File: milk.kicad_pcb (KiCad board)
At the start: 2 copper layers, 20 x 38 mm, 6 parts, among them J1 RGB, J4 RST, K1 KEYSW, K2 KEYSW, U1 ProMicro

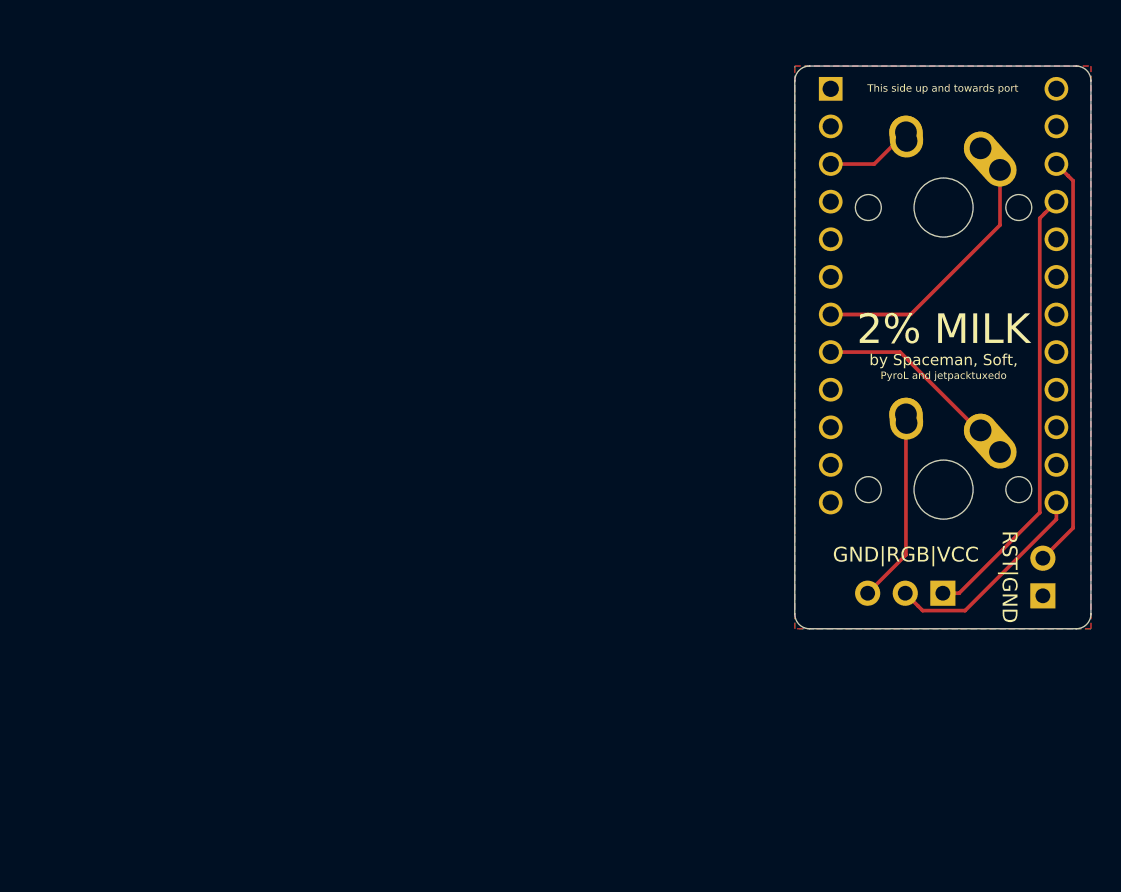
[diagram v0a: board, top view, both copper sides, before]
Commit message: initial schematic and layout (fails drc)
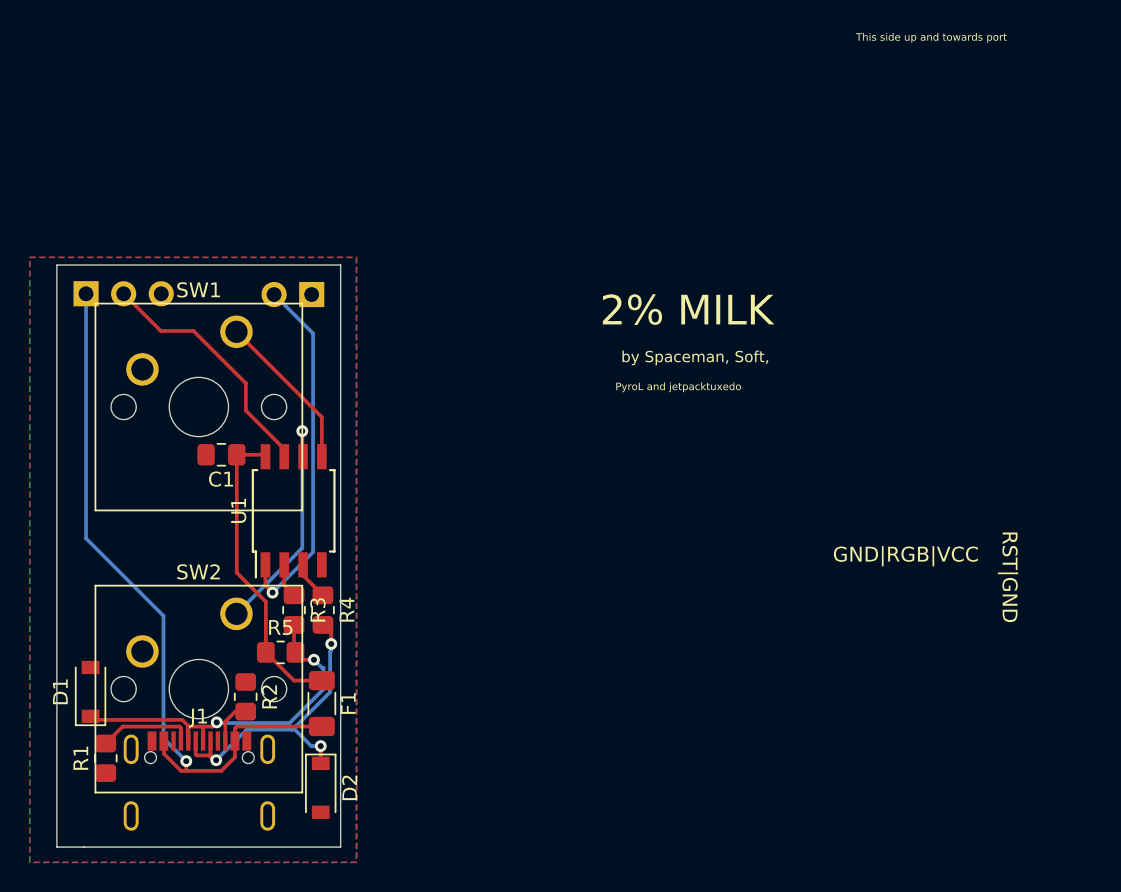
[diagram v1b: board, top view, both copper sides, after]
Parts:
- removed K1, K2: KEYSW, MX_Alps_Hybrid:MX-1U-NoLED
- added C1: 0.1uf, Capacitor_SMD:C_0805_2012Metric_Pad1.18x1.45mm_HandSolder, F.Cu at (181.3, 76.3)
- added D1: 3.6V, Diode_SMD:D_SOD-123, F.Cu at (172.4, 92.3)
- added D2: 3.6V, Diode_SMD:D_SOD-123, F.Cu at (188.0, 98.7)
- added F1: Polyfuse, Resistor_SMD:R_1206_3216Metric_Pad1.30x1.75mm_HandSolder, F.Cu at (188.1, 93.1)
- added J1: USB_C_Receptacle_USB2.0, footprints:Molex_2171800001, F.Cu at (179.8, 103.5)
- added R1: 5.1K, Resistor_SMD:R_0805_2012Metric_Pad1.20x1.40mm_HandSolder, F.Cu at (173.5, 96.7)
- added R2: 5.1K, Resistor_SMD:R_0805_2012Metric_Pad1.20x1.40mm_HandSolder, F.Cu at (182.9, 92.6)
- added R3: 68, Resistor_SMD:R_0805_2012Metric_Pad1.20x1.40mm_HandSolder, F.Cu at (186.2, 86.7)
- added R4: 68, Resistor_SMD:R_0805_2012Metric_Pad1.20x1.40mm_HandSolder, F.Cu at (188.1, 86.7)
- added R5: 1.5K, Resistor_SMD:R_0805_2012Metric_Pad1.20x1.40mm_HandSolder, F.Cu at (185.3, 89.6)
- added SW1: SW_Push, Button_Switch_Keyboard:SW_Cherry_MX_1.00u_PCB, F.Cu at (182.3, 67.9)
- added SW2: SW_Push, Button_Switch_Keyboard:SW_Cherry_MX_1.00u_PCB, F.Cu at (182.3, 87.0)
- U1: value ProMicro -> ATtiny85-20SU; footprint keyboard_parts:ProMicro_NoSilk -> Package_SO:SOIJ-8_5.3x5.3mm_P1.27mm
- moved J3 61.3 mm to (172.1, 65.4), turned to 90 degrees
- moved J2 53.4 mm to (187.4, 65.4), turned to 270 degrees
- moved U1 46.2 mm to (186.2, 80.0), turned to 90 degrees
- moved G*** 17.1 mm to (215.2, 60.5)
- renumbered J4 to J2, J1 to J3
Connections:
- J2 pad 2: /RST -> RST
- J3 pad 2: /RGB -> RGB
- U1 pad 1: Net-(U1-Pad1) -> RST
- U1 pad 2: Net-(U1-Pad2) -> PB3
- U1 pad 3: GND -> PB4
- U1 pad 7: /k1 -> RGB
- U1 pad 8: /k2 -> +5V
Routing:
- net /RST: track 27.9 -> 0.00 mm
- net D-: track 0.00 -> 25.9 mm, vias 0 -> 2
- net RST: track 0.00 -> 24.4 mm, vias 0 -> 1
- net D+: track 0.00 -> 22.0 mm, vias 0 -> 3
- net +5V: track 0.00 -> 20.7 mm
- net GND: track 19.5 -> 0.00 mm
- net VCC: track 30.3 -> 49.4 mm, vias 0 -> 1
- net /k1: track 17.7 -> 0.00 mm
- net RGB: track 0.00 -> 17.3 mm
- net Net-(SW2-Pad1): track 0.00 -> 15.9 mm, vias 0 -> 1
- net /RGB: track 14.4 -> 0.00 mm
- net /k2: track 14.2 -> 0.00 mm
- net Net-(SW1-Pad1): track 0.00 -> 10.8 mm
- net Net-(J1-PadA5): track 0.00 -> 6.47 mm
- net Net-(J1-PadB5): track 0.00 -> 2.97 mm
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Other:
- board size 20 x 38 mm -> 19.2 x 39.3 mm

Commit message: DRC ok
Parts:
- removed G***: LOGO, silks:40logo
- added ?: LOGO, silks:40logo, B.Cu at (181.1, 78.6)
- moved R2 7.81 mm to (180.7, 85.1)
- moved D1 2.84 mm to (173.7, 89.7)
- moved D2 2.84 mm to (189.3, 96.2)
- moved F1 2.84 mm to (189.3, 90.5)
- moved J2 2.84 mm to (188.6, 62.9)
- moved R3 2.84 mm to (187.5, 84.2)
- moved R4 2.84 mm to (189.4, 84.2)
- moved J3 2.84 mm to (173.4, 62.8)
- moved R5 2.84 mm to (186.6, 87.1)
- moved SW2 2.84 mm to (183.6, 84.5)
- moved C1 2.84 mm to (182.5, 73.7)
- moved U1 2.84 mm to (187.4, 77.5)
- moved J1 2.84 mm to (181.1, 101.0)
- moved R1 2.84 mm to (174.7, 94.2)
- moved SW1 2.84 mm to (183.6, 65.4)
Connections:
- J1 pad : (no net) -> GND
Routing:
- net Net-(J1-PadB5): track 2.97 -> 10.8 mm
- net GND: track 0.00 -> 3.28 mm, vias 0 -> 4
- net D-: track 25.9 -> 28.4 mm
- net RST: track 24.4 -> 25.5 mm
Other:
- board text added: "VCC|RGB|GND"
- board text removed: "GND|RGB|VCC"

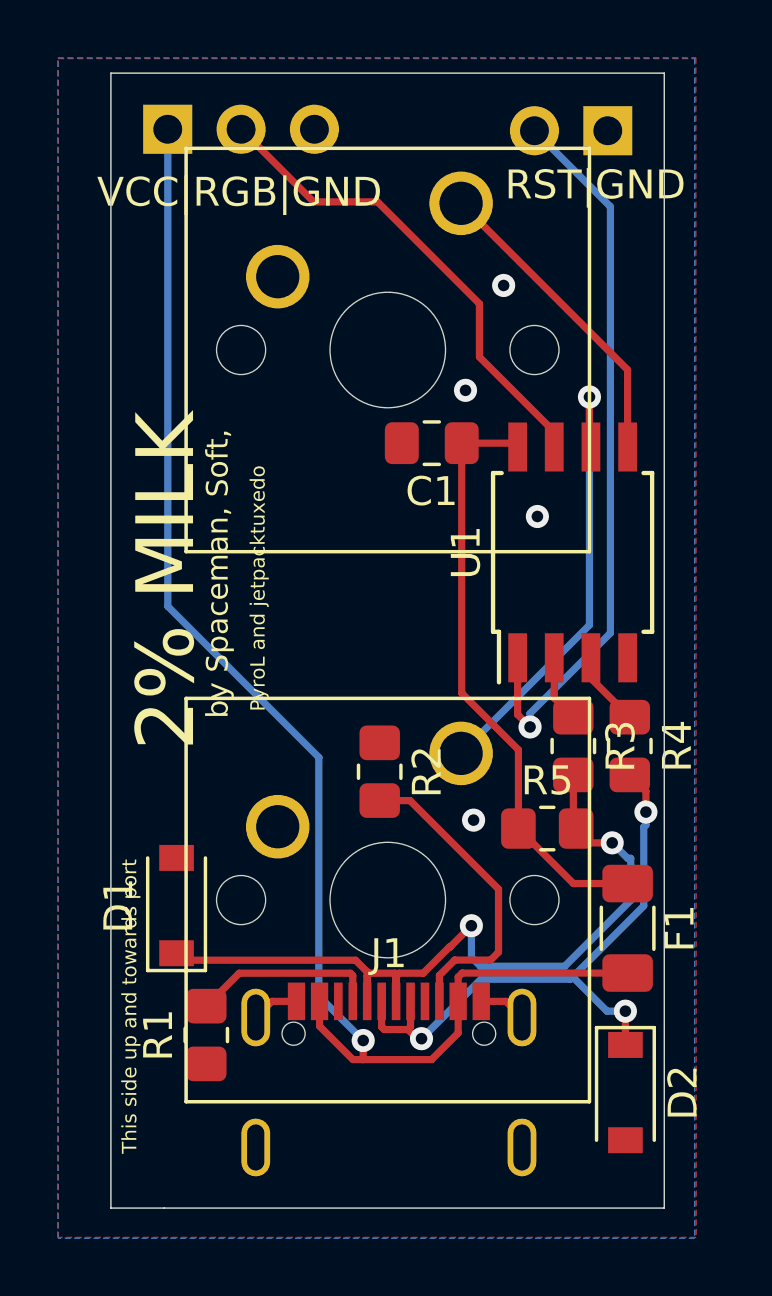
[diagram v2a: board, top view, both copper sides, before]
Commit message: Add programming headers (all over the place... yes)
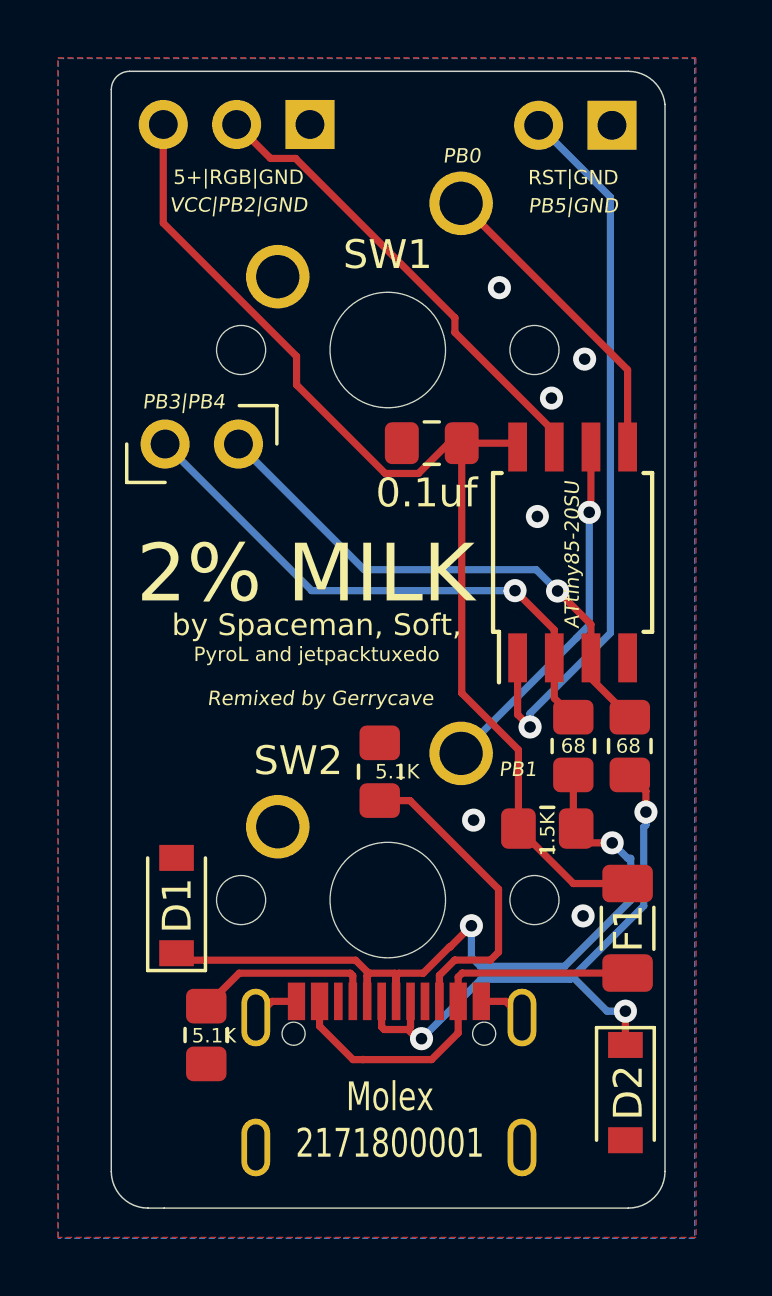
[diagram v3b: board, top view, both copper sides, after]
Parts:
- added J4: PB3|PB4, Connector_PinHeader_2.54mm:PinHeader_1x02_P2.54mm_Vertical, F.Cu at (173.3, 73.7)
- moved J3 4.93 mm to (178.3, 62.7), turned to 270 degrees
- moved J2 0.24 mm to (188.8, 62.7)
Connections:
- J3 pad 1: VCC -> GND
- J3 pad 3: GND -> +5V
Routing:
- net VCC: track 49.4 -> 14.4 mm, vias 1 -> 0
- net +5V: track 20.7 -> 39.2 mm
- net PB3: track 2.33 -> 19.4 mm, vias 0 -> 1
- net PB4: track 2.61 -> 18.6 mm, vias 0 -> 1
- net Net-(SW2-Pad1): track 15.9 -> 13.2 mm
- net RGB: track 17.3 -> 16.8 mm
- net GND: vias 4 -> 6
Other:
- board size 19.2 x 39.3 mm -> 19.2 x 39.4 mm
- rule pad_to_mask_clearance: 0.051 -> 0
- board text added: "0.1uf"
- board text added: "1.5K"
- board text added: "5+|RGB|GND"
- board text added: "5.1K"
- board text added: "68"
- board text added: "ATtiny85-20SU"
- board text added: "Molex 2171800001"
- board text added: "PB0"
- board text added: "PB1"
- board text added: "PB3|PB4"
- board text added: "PB5|GND"
- board text added: "Remixed by Gerrycave"
- board text added: "VCC|PB2|GND"
- board text removed: "This side up and towards port"
- board text removed: "VCC|RGB|GND"

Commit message: Final gerber, rendered images
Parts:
- added .: TestPoint_THTPad_D1.5mm_Drill0.7mm, TestPoint:TestPoint_THTPad_D1.5mm_Drill0.7mm, F.Cu at (180.3, 63.5)
- added .: TestPoint_THTPad_D1.5mm_Drill0.7mm, TestPoint:TestPoint_THTPad_D1.5mm_Drill0.7mm, F.Cu at (177.8, 73.7)
- moved J2 1.15 mm to (188.0, 63.5)
- moved J3 0.98 mm to (177.8, 63.5)
- moved J4 0.60 mm to (172.7, 73.7)
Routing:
- net Net-(SW2-Pad1): track 13.2 -> 26.4 mm
- net Net-(SW1-Pad1): track 10.8 -> 14.8 mm
- net PB4: track 18.6 -> 20.5 mm
- net RGB: track 16.8 -> 18.1 mm
- net PB3: track 19.4 -> 20.6 mm
- net GND: vias 6 -> 9
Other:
- board text added: "PB3|PB4|PB1"
- board text removed: "PB1"
- board text removed: "PB3|PB4"

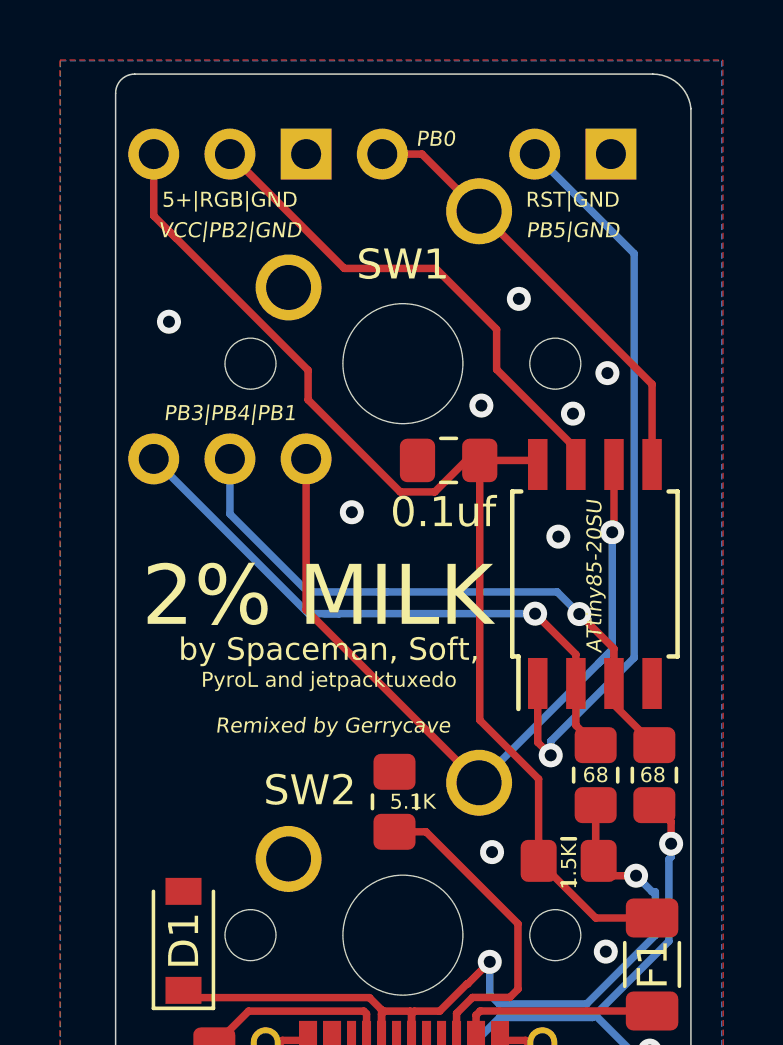
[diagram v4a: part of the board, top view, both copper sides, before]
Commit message: Fix pogo pin tht holes
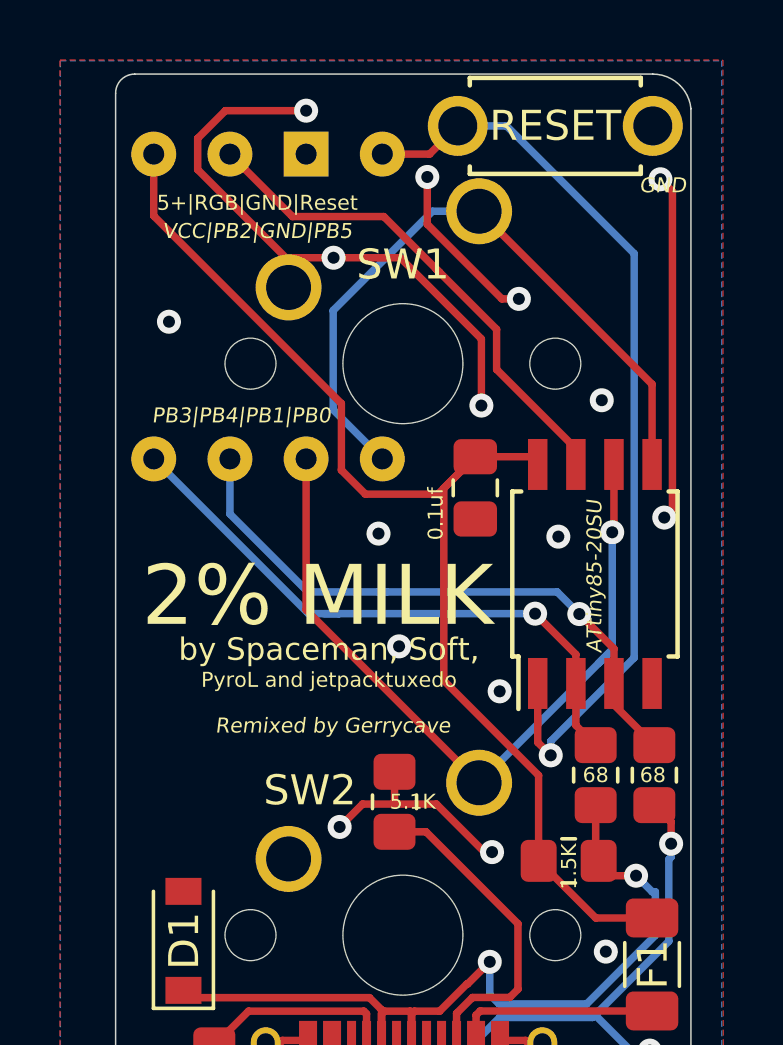
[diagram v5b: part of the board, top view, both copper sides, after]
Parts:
- removed . (x2): TestPoint_THTPad_D1.5mm_Drill0.7mm, TestPoint:TestPoint_THTPad_D1.5mm_Drill0.7mm
- removed J2: RST, Connector_PinHeader_2.54mm:PinHeader_1x02_P2.54mm_Vertical
- added H1: Switch Pin 1, TestPoint:TestPoint_THTPad_D1.5mm_Drill0.7mm, F.Cu at (180.3, 73.7)
- added H2: Switch Pin 1, TestPoint:TestPoint_THTPad_D1.5mm_Drill0.7mm, F.Cu at (177.8, 73.7)
- added H3: Reset, TestPoint:TestPoint_THTPad_D1.5mm_Drill0.7mm, F.Cu at (180.3, 63.5)
- added SW3: SW_Push_Reset, footprints:ResetSW_1side, F.Cu at (186.1, 62.6)
- moved C1 1.28 mm to (183.4, 74.6), turned to 270 degrees
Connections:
- net Net-(SW1-Pad1) renamed PB0
- net Net-(SW2-Pad1) renamed PB1
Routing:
- net GND: track 3.28 -> 46.9 mm, vias 9 -> 16
- net PB0: track 14.8 -> 22.7 mm
- net RST: track 25.1 -> 31.0 mm
- net +5V: track 39.0 -> 40.6 mm
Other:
- board text added: "5+|RGB|GND|Reset"
- board text added: "GND"
- board text added: "PB3|PB4|PB1|PB0"
- board text added: "VCC|PB2|GND|PB5"
- board text removed: "5+|RGB|GND"
- board text removed: "PB0"
- board text removed: "PB3|PB4|PB1"
- board text removed: "PB5|GND"
- board text removed: "RST|GND"
- board text removed: "VCC|PB2|GND"

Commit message: Add pull up resistor for Reset/PB5
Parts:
- added R6: 5.1K, Resistor_SMD:R_0805_2012Metric_Pad1.20x1.40mm_HandSolder, F.Cu at (180.1, 61.8)
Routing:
- net +5V: track 40.6 -> 48.0 mm
- net RST: track 31.0 -> 35.1 mm
- net GND: vias 16 -> 17
